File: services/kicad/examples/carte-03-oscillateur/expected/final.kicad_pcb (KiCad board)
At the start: 2 copper layers, 50 x 35 mm, 15 parts, among them J1 PWR, J2 OUT, U1 NE555

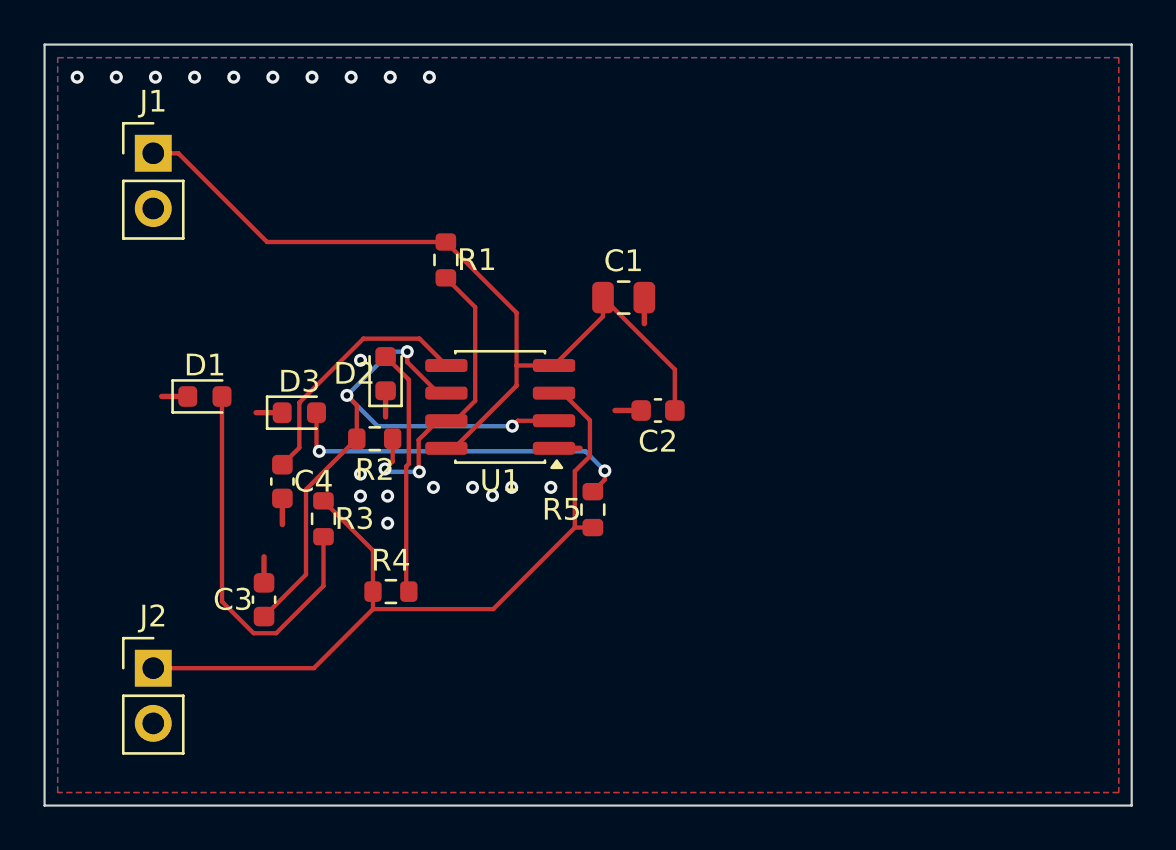
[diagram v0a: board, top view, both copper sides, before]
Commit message: feat(kicad): placement pro et routage 100 % fabricable sur les 16 cartes -- integration sur main (#164)
Branche d'integration coupee depuis origin/main (fab2a82, PR #162) : les
fichiers cles de main etaient des instantanes de feat/placement-seed-snap-
bypass (routing.py = 7981019, placement.py = 437a8b4...). On reprend donc
l'arbre entier de cette branche (345 commits, dernier 9f48667) et on y
conserve ce que main seul apportait :
- tools/verrou_routage.py + son test : « 6,2 Go par routage » rectifie
  (0,2 Go mesure ; c'est la concurrence qui emballe la memoire) ;
- tests/test_driver_llm_resync.py ;
- CLAUDE.md, PLAN.md, DECISIONS.md : fusion a trois voies, les sections
  des deux lignes conservees (2026-09-05 conteneur/verrou, 2026-09-07
  parcours asynchrone et chaine du driver, 2026-09-09/10 lecons).
Les skills *-delegate restent supprimes (remplaces le 2026-08-30).

Contenu : banc en deux phases (placement valide puis routage gele), snap
sur les regles natives, repli GND cible, journal Freerouting incremental,
horloge sans progres, via d'echappement vers le plan principal,
serigraphie degagee ; 16 cartes livrees a 100 %, 0 erreur DRC.

Verification : pytest services/kicad 1805 passed, 16 skipped ;
pnpm type-check 8/8.


Claude-Session: https://claude.ai/code/session_01TnMqm4La2CxQHHB5K8aSSV

Co-authored-by: Claude Fable 5.1 <noreply@anthropic.com>
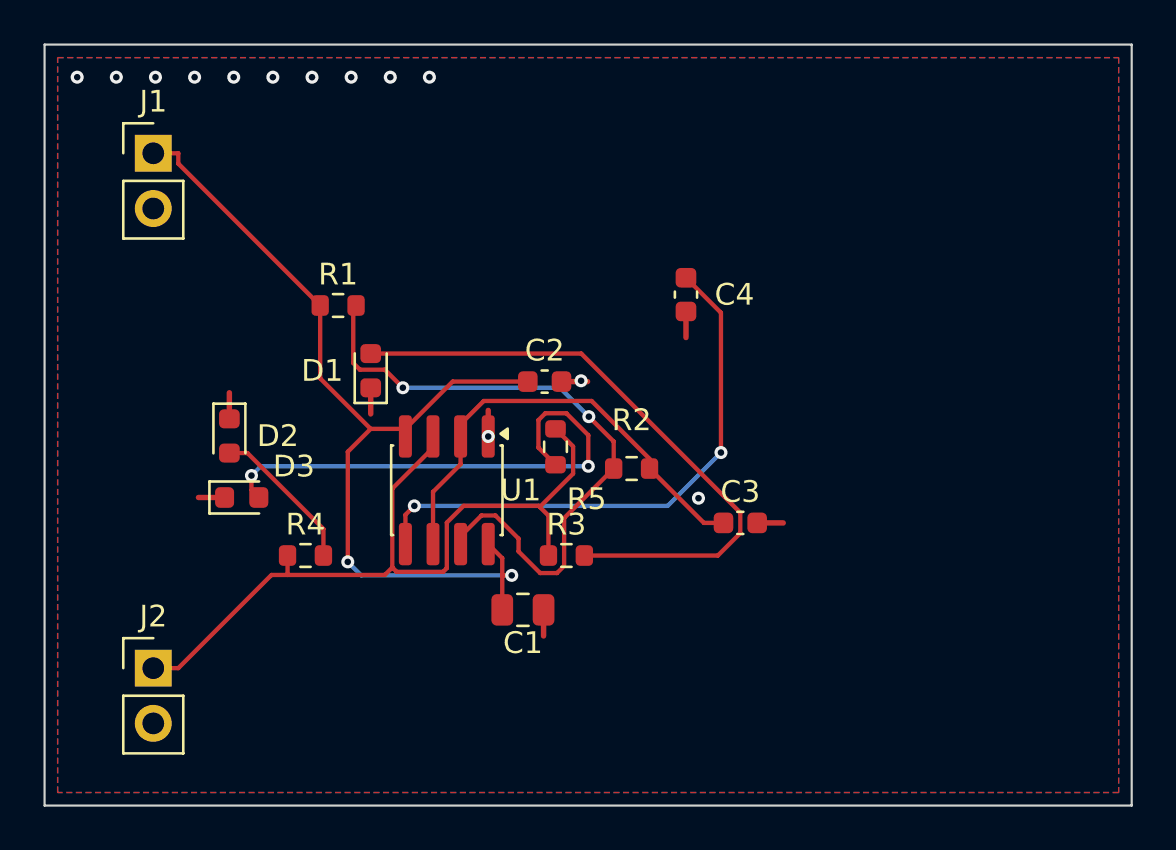
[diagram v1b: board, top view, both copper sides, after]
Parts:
- moved C3 22.2 mm to (155.5, 109.5), turned to 0 degrees
- moved C4 20.5 mm to (153.0, 99.0)
- moved C1 15.1 mm to (145.5, 113.5)
- moved R2 11.9 mm to (150.5, 107.0), turned to 0 degrees
- moved R3 11.3 mm to (147.5, 111.0), turned to 0 degrees
- moved D2 7.73 mm to (132.0, 105.5), turned to -90 degrees
- moved D1 7.72 mm to (138.5, 102.5), turned to 90 degrees
- moved R1 5.38 mm to (137.0, 99.5), turned to 0 degrees
- moved C2 5.38 mm to (146.5, 103.0), turned to 0 degrees
- moved D3 4.72 mm to (132.6, 108.3)
- moved U1 4.55 mm to (142.0, 108.0), turned to -90 degrees
- moved R4 4.26 mm to (135.5, 111.0)
- moved R5 3.36 mm to (147.0, 106.0), turned to -90 degrees
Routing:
- net DISCH: track 14.2 -> 29.9 mm
- net CTRL: track 11.7 -> 25.8 mm, vias 0 -> 2
- net LED1_A: track 17.9 -> 28.6 mm
- net THRES: track 28.8 -> 21.2 mm, vias 3 -> 0
- net LED3_A: track 16.5 -> 23.5 mm
- net LED2_A: track 11.4 -> 6.99 mm
- net VCC: track 39.9 -> 44.0 mm, vias 0 -> 2
- net OUT: track 36.2 -> 36.9 mm
- net GND: vias 20 -> 13

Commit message: chore(banc): relivrer carte-01..10 avec la couture corrigee
Boards reroutes par HTTP depuis placement.kicad_pcb inchange, avec le
code de #217. Juges par remesurer_banc.py : 0 erreur, 0 connexion
manquante sur les dix. 678 -> 443 vias ; la rangee de vias GND du bord
haut a disparu.

mesures.json : `board` recompte, `drc_du_board` rejuge, nouvelle cle
`couture_corrigee` (date, vias_avant, couches). journal.txt et les
champs du run d origine sont laisses tels quels et le disent.
rendu-3d.png : kicad-cli, modeles 3D, iso 1400x900.

Couches d un tirage : huit cartes sur 2, carte-08 et carte-10 sur 4.
CLAUDE.md et BANC_DRIVER_LLM.md recomptes. carte-11 non touchee.

Co-Authored-By: Claude Opus 5 (1M context) <noreply@anthropic.com>
Claude-Session: https://claude.ai/code/session_01TnMqm4La2CxQHHB5K8aSSV
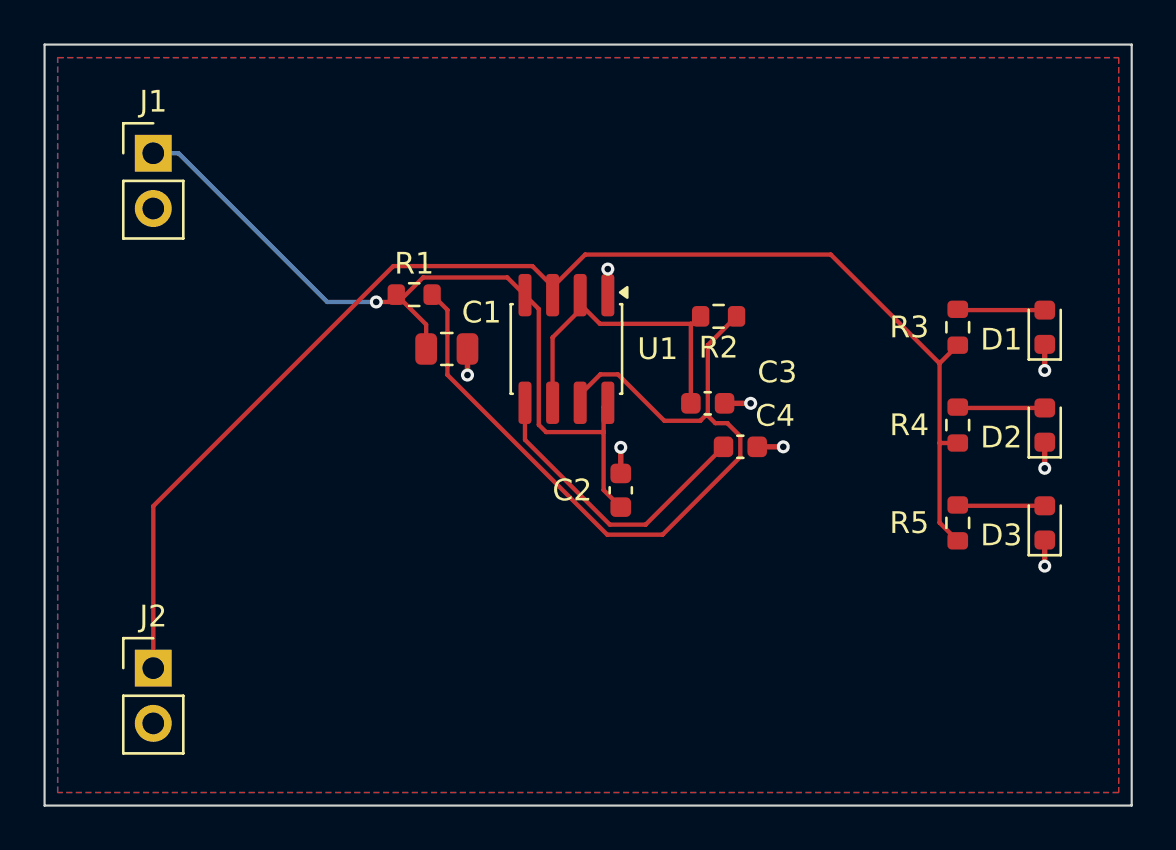
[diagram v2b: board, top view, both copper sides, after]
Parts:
- moved D2 37.5 mm to (169.5, 105.0), turned to 90 degrees
- moved D3 37.0 mm to (169.5, 109.5), turned to 90 degrees
- moved D1 31.1 mm to (169.5, 100.5)
- moved R4 30.6 mm to (165.5, 105.0), turned to 90 degrees
- moved R3 20.8 mm to (165.5, 100.5), turned to 90 degrees
- moved R5 18.8 mm to (165.5, 109.5), turned to 90 degrees
- moved C1 12.5 mm to (142.0, 101.5)
- moved U1 8.51 mm to (147.5, 101.5)
- moved R2 8.06 mm to (154.5, 100.0), turned to 180 degrees
- moved C4 7.43 mm to (155.5, 106.0), turned to 0 degrees
- moved C2 6.10 mm to (150.0, 108.0), turned to 90 degrees
- moved C3 5.70 mm to (154.0, 104.0)
- moved R1 3.54 mm to (140.5, 99.0)
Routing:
- net OUT: track 36.9 -> 62.6 mm
- net LED1_A: track 28.6 -> 4.02 mm
- net LED3_A: track 23.5 -> 4.02 mm, vias 2 -> 0
- net CTRL: track 25.8 -> 13.9 mm, vias 2 -> 0
- net DISCH: track 29.9 -> 37.6 mm, vias 2 -> 0
- net VCC: track 44.0 -> 38.2 mm, vias 2 -> 1
- net THRES: track 21.2 -> 15.4 mm
- net LED2_A: track 6.99 -> 4.02 mm
- net GND: vias 13 -> 8

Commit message: chore(banc): relivrer carte-03 et carte-06 compactes apres le correctif des angles
Rejeu complet place -> route des dix cartes par HTTP, code de #223/#224.

  carte-03  50 x 35     -> 27,8 x 19,8   0 erreur · 0 manquante
            (12 erreurs · 9 manquantes le matin, avant #224)
  carte-06  65,2 x 59,8 -> 48,4 x 36,3   0 erreur · 0 manquante

placement.kicad_pcb et final.kicad_pcb remplaces ensemble ; mesures.json
recompte et rejuge (remesurer_banc.py), cle carte_compacte ; rendus refaits.

Tableau des dix cartes dans BANC_DRIVER_LLM.md. 01/02/04/05 gardent leur
board compact du 20/09 matin (propres). 05 et 09 sortent a 1 erreur
(courtyards_overlap U2 <-> passif voisin), 07/08/10 routent desormais mais
gardent 10 a 18 connexions manquantes : non relivrees.

Co-Authored-By: Claude Fable 5.1 <noreply@anthropic.com>
Claude-Session: https://claude.ai/code/session_01TnMqm4La2CxQHHB5K8aSSV
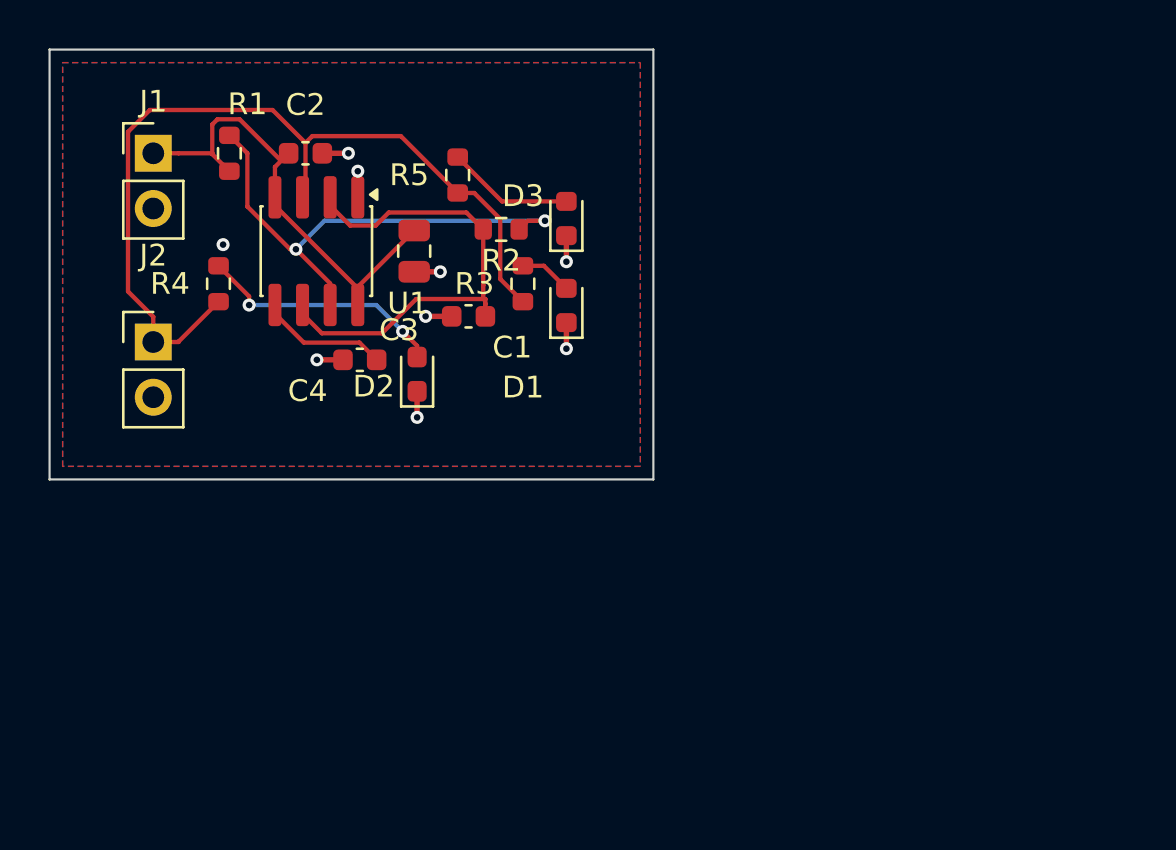
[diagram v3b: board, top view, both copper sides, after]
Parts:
- moved R4 34.6 mm to (131.5, 98.5)
- moved D2 29.0 mm to (140.6, 102.7)
- moved R5 28.0 mm to (142.5, 93.5)
- moved D3 26.1 mm to (147.5, 95.5)
- moved D1 22.0 mm to (147.5, 99.5)
- moved C2 21.2 mm to (135.5, 92.5), turned to 0 degrees
- moved R3 20.1 mm to (145.5, 98.5)
- moved C4 18.0 mm to (138.0, 102.0), turned to 180 degrees
- moved J2 15.0 mm to (128.5, 101.2)
- moved U1 12.3 mm to (136.0, 97.0)
- moved C3 11.7 mm to (143.0, 100.0), turned to 180 degrees
- moved R2 10.8 mm to (144.5, 96.0)
- moved R1 10.7 mm to (132.0, 92.5), turned to 90 degrees
- moved C1 4.74 mm to (140.5, 97.0), turned to -90 degrees
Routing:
- net OUT: track 62.6 -> 40.6 mm
- net VCC: track 38.2 -> 21.8 mm, vias 1 -> 0
- net DISCH: track 37.6 -> 23.2 mm, vias 0 -> 2
- net CTRL: track 13.9 -> 5.96 mm
- net LED2_A: track 4.02 -> 11.4 mm, vias 0 -> 2
- net THRES: track 15.4 -> 22.2 mm
- net LED3_A: track 4.02 -> 5.84 mm
- net LED1_A: track 4.02 -> 2.43 mm
- net GND: vias 8 -> 9
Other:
- board size 50 x 35 mm -> 27.8 x 19.8 mm

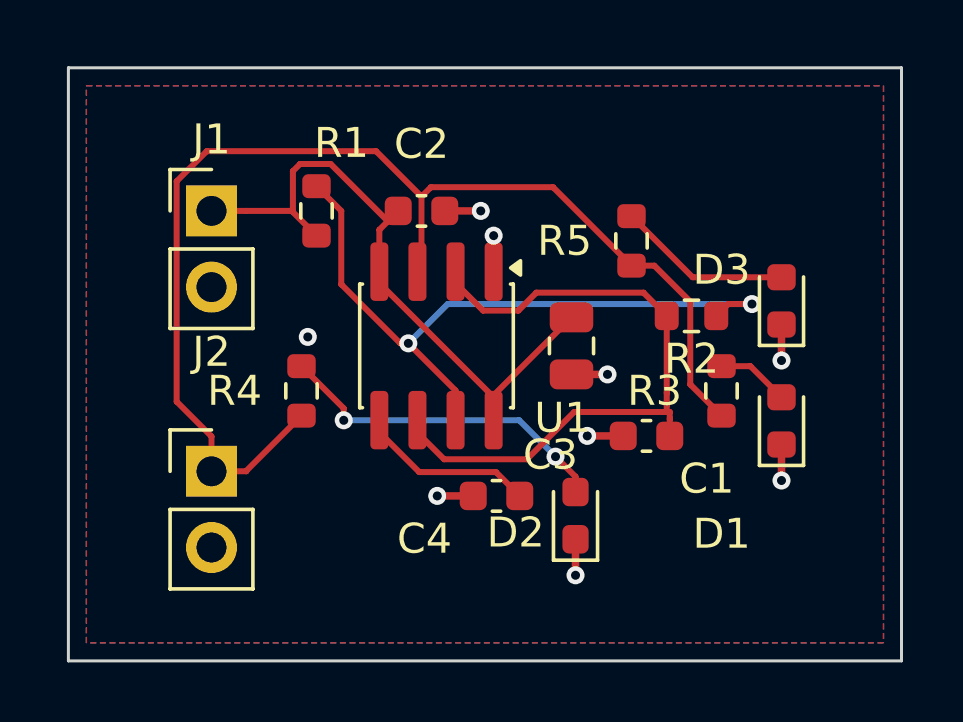
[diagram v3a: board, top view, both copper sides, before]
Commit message: fix(banc): le contour n etait JAMAIS resserre — dix cartes divisees par 2 a 4
Question de l utilisateur devant les rendus : « tu es satisfait de ce
placement ? ». Non, et la mesure lui donnait raison.

    carte-10 livree     140 x 105 mm = 14725 mm2
    son circuit          51 x  66 mm =  3366 mm2
    OCCUPATION                            23 %
    connecteurs                      56 a 75 mm du circuit
    fil de signal                      1230 mm  (VIN a lui seul 112 mm)

LA CAUSE : `run_pipeline.py` n envoyait pas `auto_size_board` a `/place/auto`.
Le resserrement du contour sur le placement existe depuis le 2026-09-13 et ne
s execute que si l appelant l autorise ; le defaut du modele est `False`.

C est le SEPTIEME levier de ce projet qui existe et que personne n appelle,
apres max_distance_mm, anchor_pin, WorkflowConfig.grid, constraints,
move_reference, bottom_up_placement et LocalRerouter.

⚠️ Et il etait INVISIBLE : la chaine de PRODUCTION passe bien le drapeau depuis
`handlePlacement`. Le banc mesurait donc un comportement que le produit n a
pas — l inverse exact de ce a quoi sert un banc.

MESURE APRES CORRECTION, meme circuit, meme graine :

    carte             demandee      REELLE        err  manq
    carte-01           25 x 20     20,1 x 14,6     0    0
    carte-02           55 x 40     34,9 x 25,4     0    0
    carte-03           50 x 35     26,1 x 20,1     0    0
    carte-04           60 x 45     36,6 x 27,2     0    0
    carte-05           70 x 50     43,6 x 32,6     0    0
    carte-06           80 x 60     48,5 x 36,4     0    0
    carte-07          110 x 80     53,2 x 38,8     0    0
    carte-08          125 x 95     56,4 x 44,1     0    0
    carte-09          130 x 100    57,3 x 45,2     0    0
    carte-10          140 x 105    61,0 x 45,8     0    0

Dix sur dix, 100 % route, aucune erreur, aucune connexion manquante. Sur
carte-10 : occupation 23 -> 56 %, fil de signal 1230 -> 652 mm, VIN 112 -> 45,5,
connecteurs 56-75 -> 23-35 mm.

ET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
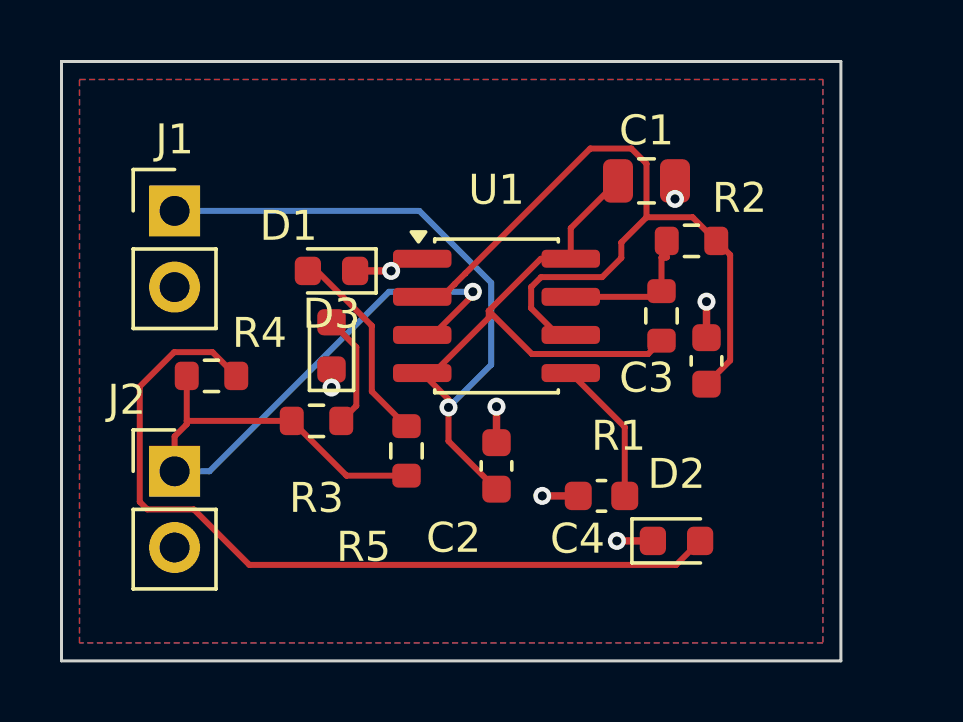
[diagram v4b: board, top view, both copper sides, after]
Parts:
- moved D1 15.2 mm to (132.5, 97.0)
- moved D3 15.0 mm to (132.5, 94.5), turned to 180 degrees
- moved R3 13.5 mm to (132.0, 99.5), turned to 0 degrees
- moved R1 12.0 mm to (143.5, 96.0)
- moved R5 10.3 mm to (135.0, 100.5)
- moved C2 8.86 mm to (138.0, 101.0), turned to 90 degrees
- moved C1 6.04 mm to (143.0, 91.5), turned to 0 degrees
- moved C4 3.50 mm to (141.5, 102.0)
- moved D2 3.47 mm to (144.0, 103.5), turned to 0 degrees
- moved C3 3.20 mm to (145.0, 97.5), turned to 90 degrees
- moved R4 3.04 mm to (128.5, 98.0), turned to 0 degrees
- moved R2 2.50 mm to (144.5, 93.5), turned to 0 degrees
- moved U1 2.24 mm to (138.0, 96.0), turned to 0 degrees
- moved J1 1.23 mm to (127.3, 92.5)
- moved J2 1.23 mm to (127.3, 101.2)
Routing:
- net DISCH: track 23.2 -> 4.95 mm, vias 2 -> 0
- net LED2_A: track 11.4 -> 27.7 mm, vias 2 -> 0
- net VCC: track 21.8 -> 37.5 mm, vias 0 -> 1
- net OUT: track 40.6 -> 26.2 mm, vias 0 -> 1
- net THRES: track 22.2 -> 27.0 mm
- net GND: track 9.60 -> 7.20 mm, vias 9 -> 7
- net LED1_A: track 2.43 -> 3.84 mm
- net CTRL: track 5.96 -> 4.84 mm
- net LED3_A: track 5.84 -> 6.71 mm
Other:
- board size 27.8 x 19.8 mm -> 26 x 20 mm
